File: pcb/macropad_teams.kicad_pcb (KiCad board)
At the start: 2 copper layers, 140 x 72.5 mm, 32 parts, among them J1 Conn_01x04, SW1 SW_Push, SW10 SW_Push, SW11 SW_Push, SW12 SW_Push, SW13 SW_Push, SW14 SW_Push, SW2 SW_Push, SW3 SW_Push, SW4 SW_Push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

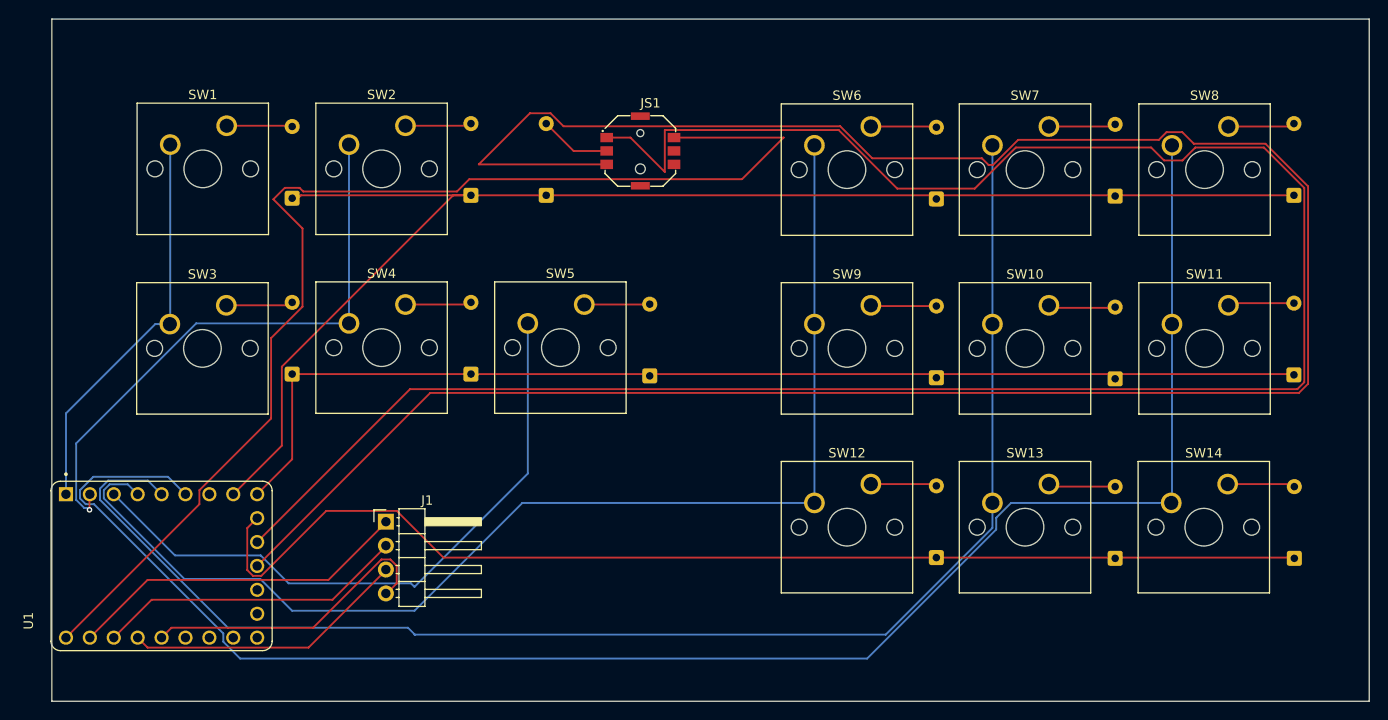
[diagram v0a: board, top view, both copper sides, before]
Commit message: On branch main Changes to be committed: deleted:    pcb/macropad_teams-backups/macropad_teams-2025-10-22_212323.zip deleted:    pcb/macropad_teams-backups/macropad_teams-2025-10-22_213140.zip deleted:    pcb/macropad_teams-backups/macropad_teams-2025-10-22_213929.zip modified:   pcb/macropad_teams.kicad_pcb
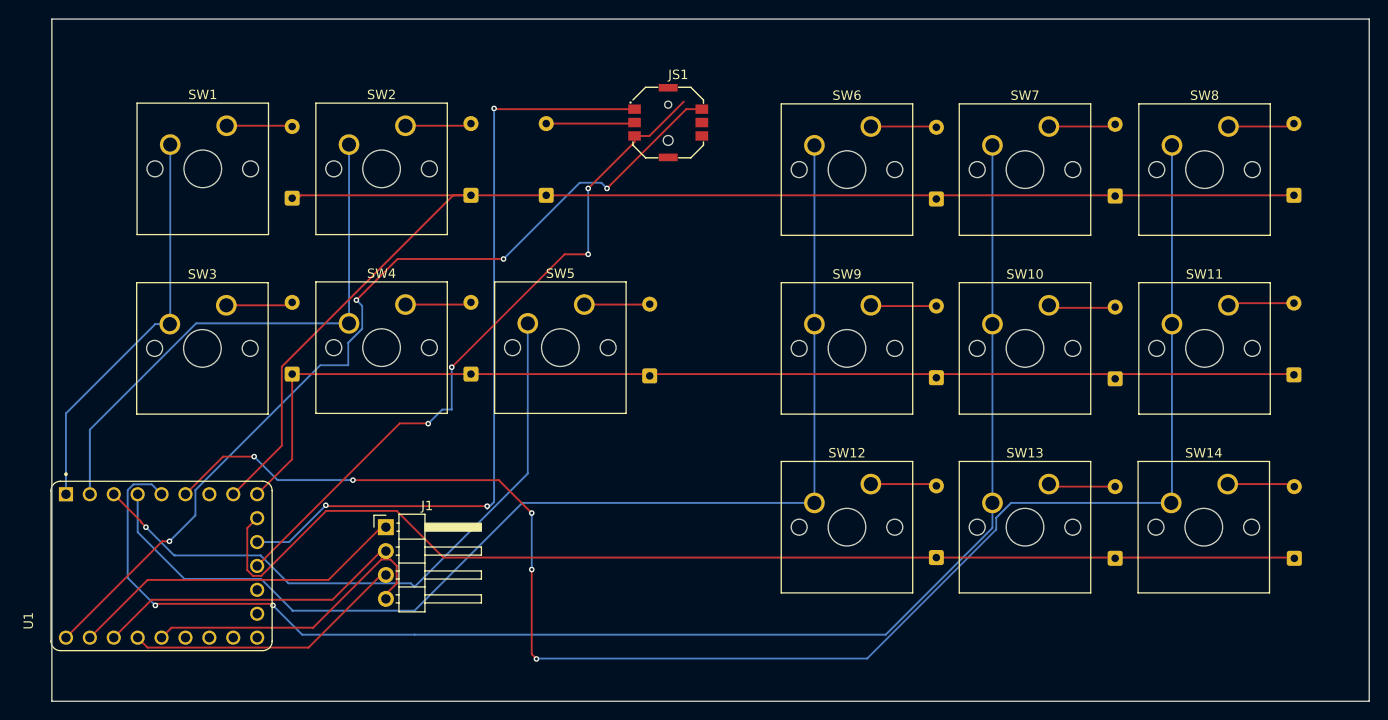
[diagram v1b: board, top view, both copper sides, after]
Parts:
- moved JS1 4.23 mm to (147.0, 71.0)
- moved J1 0.58 mm to (117.0, 114.0)
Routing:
- net /JS_Y: track 250.8 -> 72.9 mm, vias 0 -> 4
- net /JS_X: track 226.4 -> 84.3 mm, vias 0 -> 3
- net /JS1VCC: track 127.2 -> 97.0 mm, vias 0 -> 4
- net /col5: track 182.6 -> 169.7 mm, vias 0 -> 5
- net /col3: track 128.4 -> 122.2 mm
- net /col1: track 63.0 -> 58.1 mm, vias 1 -> 0
- net Net-(D15-A): track 7.63 -> 9.43 mm
- net /col4: track 154.9 -> 153.5 mm, vias 0 -> 2
- net /col2: track 69.0 -> 69.1 mm, vias 0 -> 1

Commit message: On branch main  Changes to be committed: 	deleted:    pcb/macropad_teams-backups/macropad_teams-2025-10-26_193725.zip 	deleted:    pcb/macropad_teams-backups/macropad_teams-2025-10-26_194634.zip 	modified:   pcb/macropad_teams.kicad_pcb
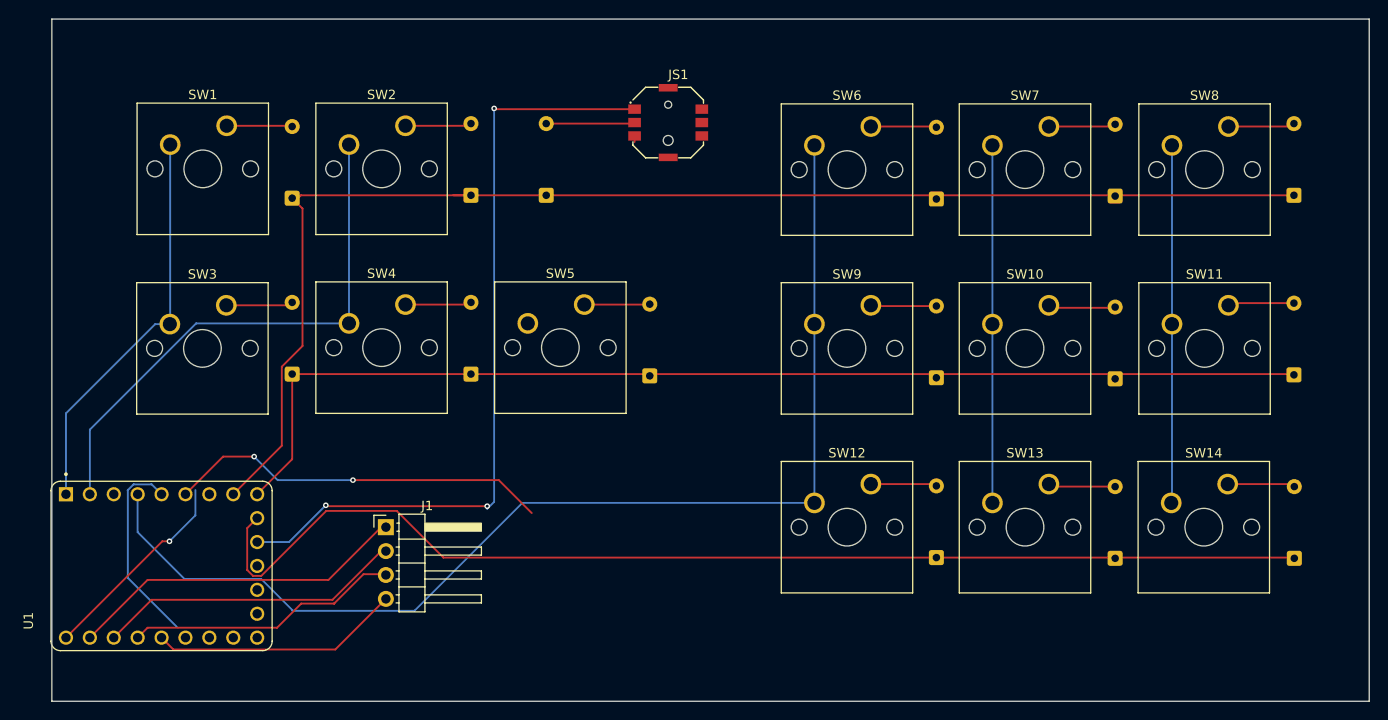
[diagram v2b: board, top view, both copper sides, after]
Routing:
- net /col4: track 153.5 -> 59.1 mm, vias 2 -> 0
- net /col5: track 169.7 -> 79.0 mm, vias 5 -> 2
- net /JS1VCC: track 97.0 -> 21.8 mm, vias 4 -> 1
- net /JS_Y: track 72.9 -> 0.65 mm, vias 4 -> 0
- net /col2: track 69.1 -> 0.00 mm, vias 1 -> 0
- net row0: track 150.4 -> 143.9 mm
- net /SDA: track 32.2 -> 26.6 mm
- net /SCL: track 30.2 -> 29.2 mm

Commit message: On branch main Changes to be committed: deleted:    pcb/macropad_teams-backups/macropad_teams-2025-10-26_201154.zip deleted:    pcb/macropad_teams-backups/macropad_teams-2025-10-26_203901.zip deleted:    pcb/macropad_teams-backups/macropad_teams-2025-10-26_204439.zip modified:   pcb/macropad_teams.kicad_pcb modified:   pcb/macropad_teams.kicad_prl modified:   pcb/macropad_teams.kicad_sch
Much neater PCB routing this time around
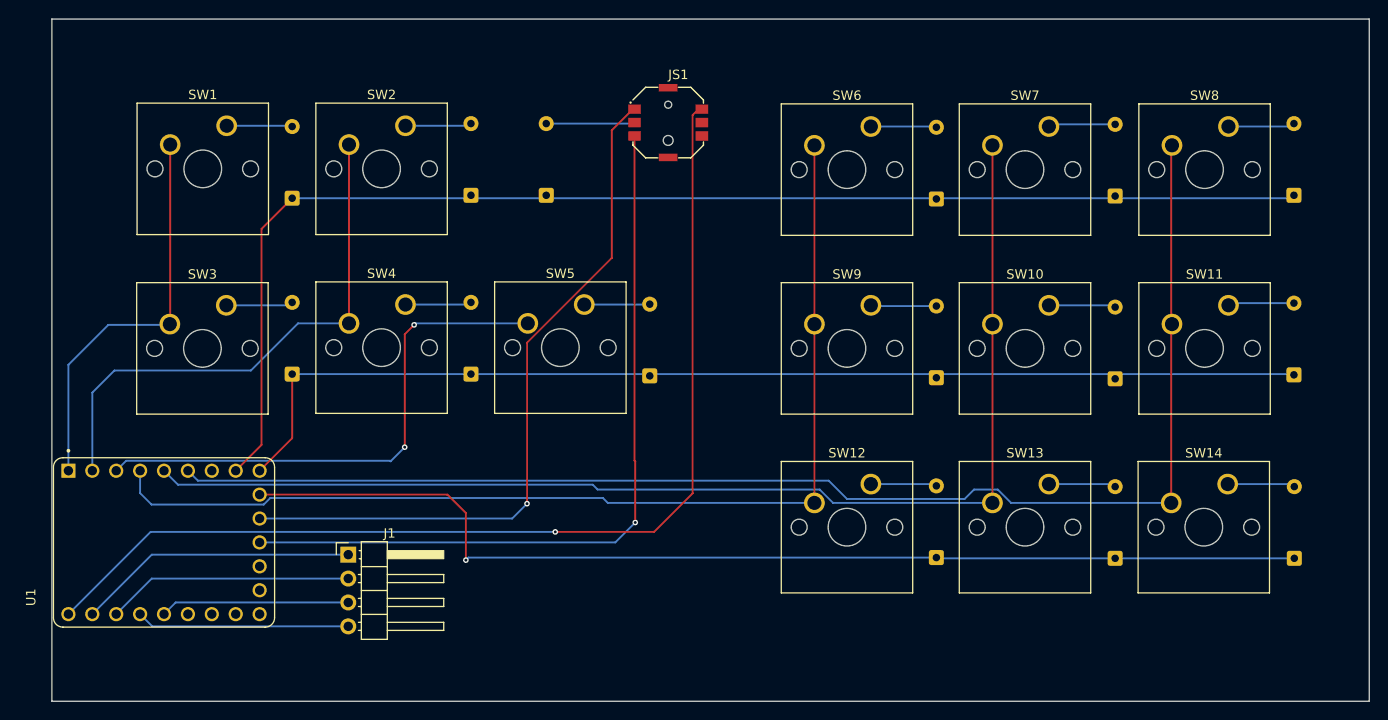
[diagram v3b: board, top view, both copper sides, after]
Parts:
- moved J1 4.95 mm to (113.0, 116.9)
- moved U1 2.51 mm to (93.4, 115.6)
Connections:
- U1 pad 19: /SDA -> /SCL
- U1 pad 20: /SCL -> /SDA
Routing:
- net /JS1VCC: track 21.8 -> 113.1 mm
- net /JS_Y: track 0.65 -> 81.9 mm, vias 0 -> 1
- net /col4: track 59.1 -> 127.5 mm
- net /col5: track 79.0 -> 144.8 mm, vias 2 -> 0
- net /col2: track 0.00 -> 57.3 mm, vias 0 -> 2
- net /col3: track 122.2 -> 113.0 mm
- net /SCL: track 29.2 -> 20.1 mm
- net /JS_X: track 84.3 -> 75.8 mm, vias 3 -> 1
- net /GND: track 36.5 -> 29.8 mm
- net /3V3: track 32.9 -> 26.2 mm
- net row2: track 122.4 -> 115.9 mm, vias 0 -> 1
- net row0: track 143.9 -> 138.0 mm
- net /SDA: track 26.6 -> 22.7 mm
- net row1: track 120.8 -> 118.2 mm
- net /col1: track 58.1 -> 57.6 mm

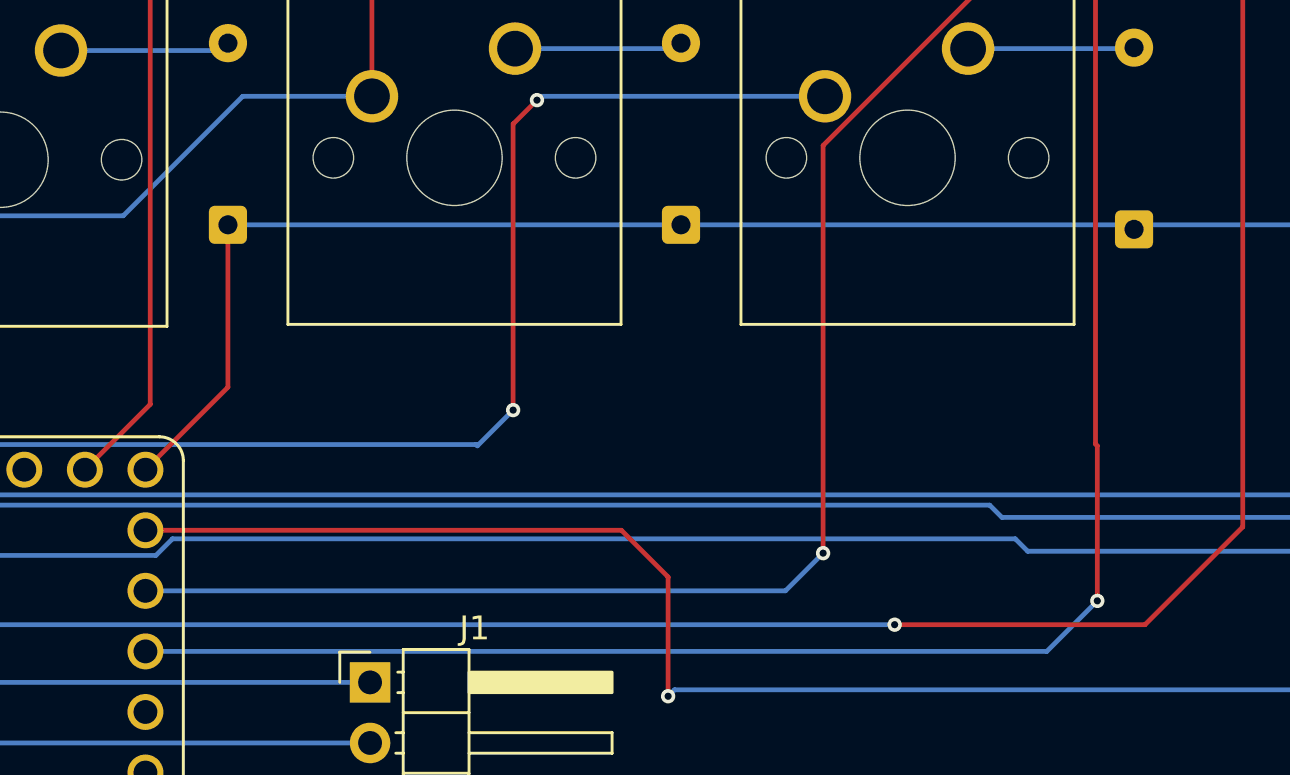
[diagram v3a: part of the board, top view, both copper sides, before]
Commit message: On branch main  Changes to be committed: 	deleted:    pcb/macropad_teams-backups/macropad_teams-2025-10-28_144739.zip 	modified:   pcb/macropad_teams.kicad_pcb
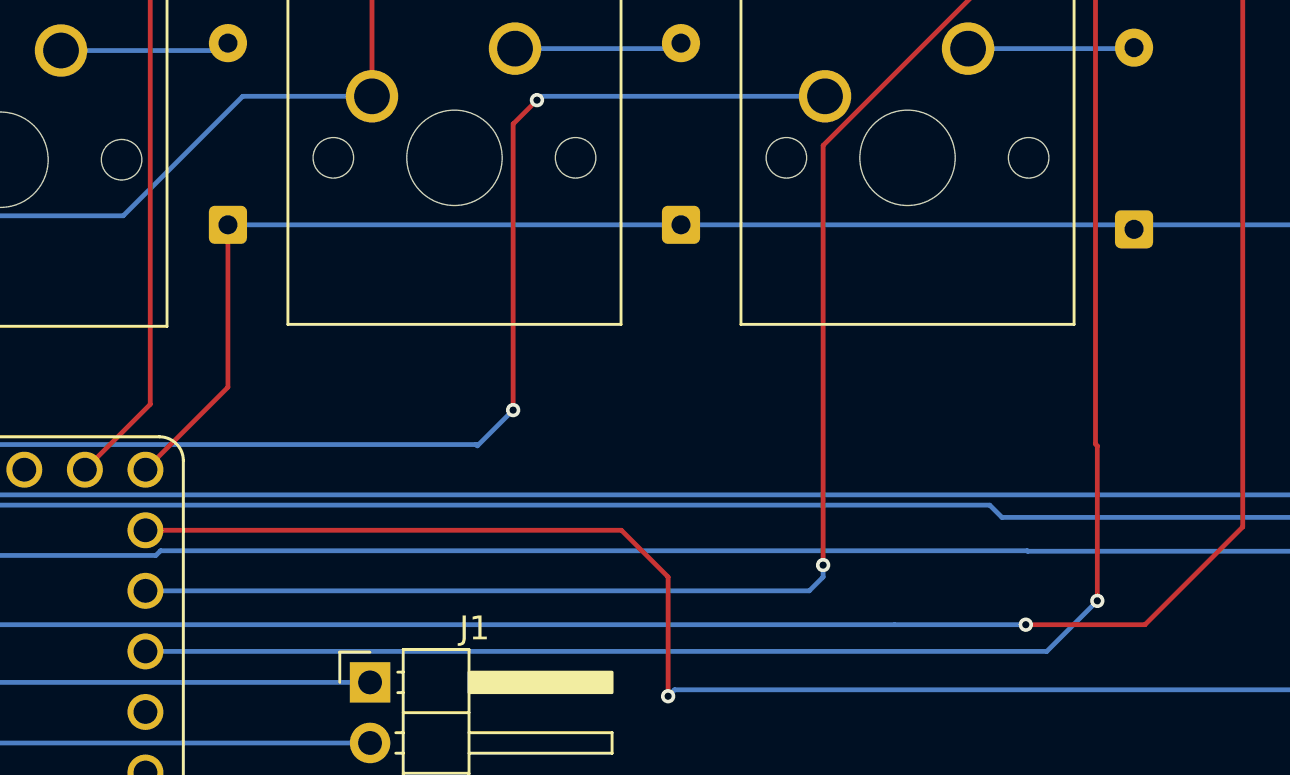
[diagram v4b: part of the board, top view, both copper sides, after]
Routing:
- net /JS_X: track 75.8 -> 76.4 mm
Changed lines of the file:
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@@
-	)
-	(segment
-		(start 140.059 110.899)
-		(end 104.712996 110.899)
-		(width 0.2)
-		(layer "B.Cu")
-		(net 31)
-	)
-	(segment
-		(start 140.58 111.42)
-		(end 140.059 110.899)
-		(width 0.2)
-		(layer "B.Cu")
-		(net 31)
 	)
 	(segment
@@
 	)
 	(segment
+		(start 104.212996 111.399)
+		(end 104.016996 111.595)
+		(width 0.2)
+		(layer "B.Cu")
+		(net 31)
+	)
+	(segment
+		(start 140.559 111.399)
+		(end 104.212996 111.399)
+		(width 0.2)
+		(layer "B.Cu")
+		(net 31)
+	)
+	(segment
+		(start 140.58 111.42)
+		(end 140.559 111.399)
+		(width 0.2)
+		(layer "B.Cu")
+		(net 31)
+	)
+	(segment
 		(start 162.54 111.42)
 		(end 140.58 111.42)
-		(width 0.2)
-		(layer "B.Cu")
-		(net 31)
-	)
-	(segment
-		(start 104.712996 110.899)
-		(end 104.016996 111.595)
 		(width 0.2)
 		(layer "B.Cu")
@@
 	)
 	(segment
+		(start 141 85.401314)
+		(end 141 71.825)
+		(width 0.2)
+		(layer "F.Cu")
+		(net 36)
+	)
+	(segment
+		(start 141 71.825)
+		(end 143.25 69.575)
+		(width 0.2)
+		(layer "F.Cu")
+		(net 36)
+	)
+	(segment
+		(start 132 94.401314)
+		(end 141 85.401314)
+		(width 0.2)
+		(layer "F.Cu")
+		(net 36)
+	)
+	(segment
 		(start 143.25 69.575)
 		(end 143.425 69.575)
@@
 	)
 	(segment
-		(start 132 111.5)
-		(end 132 94.401314)
-		(width 0.2)
-		(layer "F.Cu")
-		(net 36)
-	)
-	(segment
-		(start 141 71.825)
-		(end 143.25 69.575)
-		(width 0.2)
-		(layer "F.Cu")
-		(net 36)
-	)
-	(segment
-		(start 141 85.401314)
-		(end 141 71.825)
-		(width 0.2)
-		(layer "F.Cu")
-		(net 36)
-	)
-	(segment
 		(start 132 94.401314)
-		(end 141 85.401314)
+		(end 132 112)
 		(width 0.2)
 		(layer "F.Cu")
@@
 	)
 	(via
-		(at 132 111.5)
+		(at 132 112)
 		(size 0.6)
 		(drill 0.3)
@@
 	)
 	(segment
-		(start 132 111.5)
-		(end 130.42 113.08)
-		(width 0.2)
-		(layer "B.Cu")
-		(net 36)
-	)
-	(segment
-		(start 130.42 113.08)
-		(end 103.58 113.08)
-		(width 0.2)
-		(layer "B.Cu")
-		(net 36)
-	)
-	(segment
-		(start 145.5 114.5)
-		(end 135 114.5)
-		(width 0.2)
-		(layer "F.Cu")
-		(net 37)
+		(start 131.42 113.08)
+		(end 132 112.5)
+		(width 0.2)
+		(layer "B.Cu")
+		(net 36)
+	)
+	(segment
+		(start 132 112)
+		(end 132 112.5)
+		(width 0.2)
+		(layer "B.Cu")
+		(net 36)
+	)
+	(segment
+		(start 103.58 113.08)
+		(end 131.42 113.08)
+		(width 0.2)
+		(layer "B.Cu")
+		(net 36)
 	)
 	(segment
@@
 		(net 37)
 	)
+	(segment
+		(start 140.5 114.5)
+		(end 145.5 114.5)
+		(width 0.2)
+		(layer "F.Cu")
+		(net 37)
+	)
 	(via
-		(at 135 114.5)
+		(at 140.5 114.5)
 		(size 0.6)
 		(drill 0.3)
@@
 		(width 0.2)
 		(layer "B.Cu")
+		(net 37)
+	)
+	(segment
+		(start 135 114.5)
+		(end 140.5 114.5)
+		(width 0.2)
+		(layer "B.Cu")

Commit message: On branch main  Changes to be committed: 	deleted:    pcb/macropad_teams-backups/macropad_teams-2025-10-28_145826.zip 	modified:   pcb/macropad_teams.kicad_pcb
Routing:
- net row2: track 115.9 -> 115.1 mm
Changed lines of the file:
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@@
 	)
 	(segment
-		(start 123.54 110.54)
-		(end 103.58 110.54)
+		(start 125.5 112.5)
+		(end 125.5 116.5)
 		(width 0.2)
 		(layer "F.Cu")
@@
 	)
 	(segment
-		(start 125.5 117.5)
-		(end 125.5 112.5)
+		(start 123.54 110.54)
+		(end 103.58 110.54)
 		(width 0.2)
 		(layer "F.Cu")
@@
 	)
 	(via
-		(at 125.5 117.5)
+		(at 125.5 116.5)
 		(size 0.6)
 		(drill 0.3)
@@
 	(segment
 		(start 175.5 117.23)
-		(end 125.77 117.23)
+		(end 126.23 117.23)
 		(width 0.2)
 		(layer "B.Cu")
@@
 	)
 	(segment
-		(start 125.77 117.23)
-		(end 125.5 117.5)
+		(start 126.23 117.23)
+		(end 125.5 116.5)
 		(width 0.2)
 		(layer "B.Cu")
